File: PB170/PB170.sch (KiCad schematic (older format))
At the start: 30 parts, among them J1 USB_C_Receptacle_USB2.0-Conne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, J2 USB_B_Micro, Q1 P-MOSFET-MLP_HS, Q2 BC817, SW1 SW_MEC_5E, SW2 SW_MEC_5E, U1 74HC00

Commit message: Added PCB.
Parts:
- added H1, H2, H3, H4: MountingHole_Pad, Mounting_Holes:MountingHole_3.2mm_M3_Pad, symbol Mechanical:MountingHole_Pad
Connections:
- wire segments 78 -> 76
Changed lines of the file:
@@
 Wire Wire Line
 	2200 1950 2300 1950
-Wire Wire Line
-	2200 2150 2250 2150
-$Comp
-L power:PWR_FLAG #FLG0101
-U 1 1 5FD0908A
-P 2250 2150
-F 0 "#FLG0101" H 2250 2225 50  0001 C CNN
-F 1 "PWR_FLAG" H 2250 2323 50  0000 C CNN
-F 2 "" H 2250 2150 50  0001 C CNN
-F 3 "~" H 2250 2150 50  0001 C CNN
-	1    2250 2150
-	-1   0    0    1
-$EndComp
-Connection ~ 2250 2150
-Wire Wire Line
-	2250 2150 2300 2150
-$Comp
-L power:PWR_FLAG #FLG0102
-U 1 1 5FD097DA
-P 1300 2100
-F 0 "#FLG0102" H 1300 2175 50  0001 C CNN
-F 1 "PWR_FLAG" H 1300 2273 50  0000 C CNN
-F 2 "" H 1300 2100 50  0001 C CNN
-F 3 "~" H 1300 2100 50  0001 C CNN
-	1    1300 2100
-	-1   0    0    1
-$EndComp
 $Comp
 L power:+5V #PWR0104
@@
 Wire Wire Line
 	1300 2050 1300 2000
-Wire Wire Line
-	1300 2100 1300 2050
-Connection ~ 1300 2050
 Wire Notes Line
 	950  4450 3250 4450
@@
 Wire Wire Line
 	2300 6450 2600 6450
+Wire Wire Line
+	2200 2150 2300 2150
+$Comp
+L Mechanical:MountingHole_Pad H1
+U 1 1 5FD54CAB
+P 4900 7050
+F 0 "H1" H 5000 7099 50  0000 L CNN
+F 1 "MountingHole_Pad" H 5000 7008 50  0000 L CNN
+F 2 "Mounting_Holes:MountingHole_3.2mm_M3_Pad" H 4900 7050 50  0001 C CNN
+F 3 "~" H 4900 7050 50  0001 C CNN
+	1    4900 7050
+	1    0    0    -1
+$EndComp
+$Comp
+L Mechanical:MountingHole_Pad H2
+U 1 1 5FD576B7
+P 5150 7050
+F 0 "H2" H 5250 7099 50  0000 L CNN
+F 1 "MountingHole_Pad" H 5250 7008 50  0000 L CNN
+F 2 "Mounting_Holes:MountingHole_3.2mm_M3_Pad" H 5150 7050 50  0001 C CNN
+F 3 "~" H 5150 7050 50  0001 C CNN
+	1    5150 7050
+	1    0    0    -1
+$EndComp
+$Comp
+L Mechanical:MountingHole_Pad H3
+U 1 1 5FD5794D
+P 5400 7050
+F 0 "H3" H 5500 7099 50  0000 L CNN
+F 1 "MountingHole_Pad" H 5500 7008 50  0000 L CNN
+F 2 "Mounting_Holes:MountingHole_3.2mm_M3_Pad" H 5400 7050 50  0001 C CNN
+F 3 "~" H 5400 7050 50  0001 C CNN
+	1    5400 7050
+	1    0    0    -1
+$EndComp
+$Comp
+L Mechanical:MountingHole_Pad H4
+U 1 1 5FD57BD8
+P 5650 7050
+F 0 "H4" H 5750 7099 50  0000 L CNN
+F 1 "MountingHole_Pad" H 5750 7008 50  0000 L CNN
+F 2 "Mounting_Holes:MountingHole_3.2mm_M3_Pad" H 5650 7050 50  0001 C CNN
+F 3 "~" H 5650 7050 50  0001 C CNN
+	1    5650 7050
+	1    0    0    -1
+$EndComp
 $EndSCHEMATC

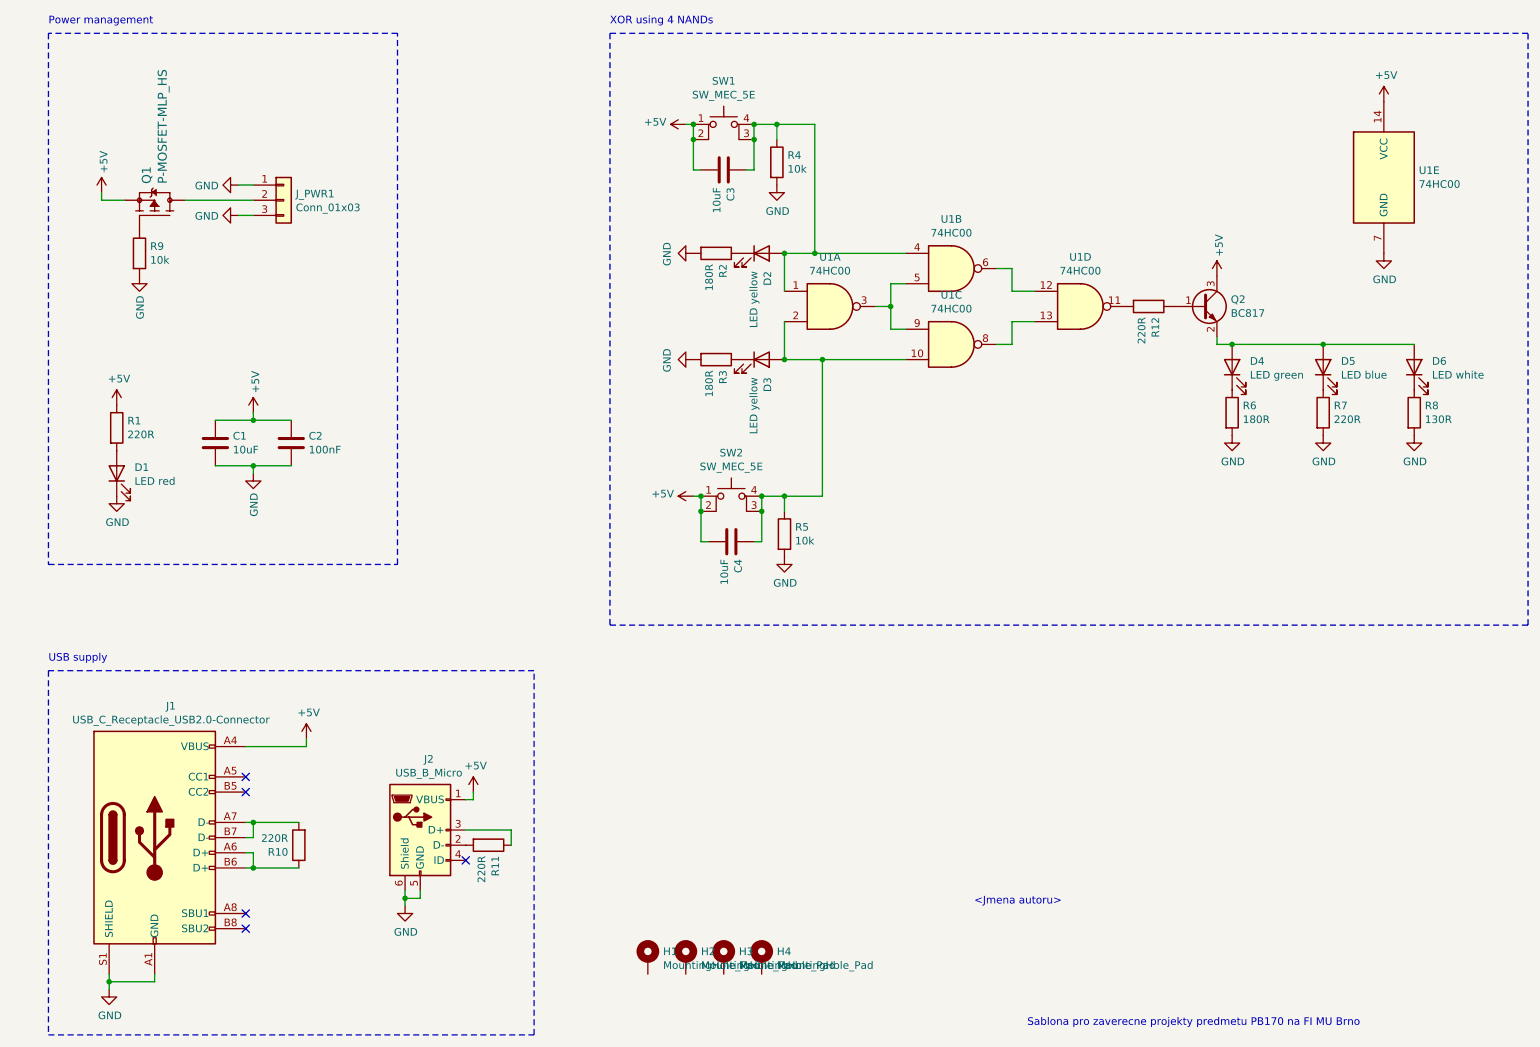
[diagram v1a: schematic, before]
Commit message: Added hierarchical sheet example.
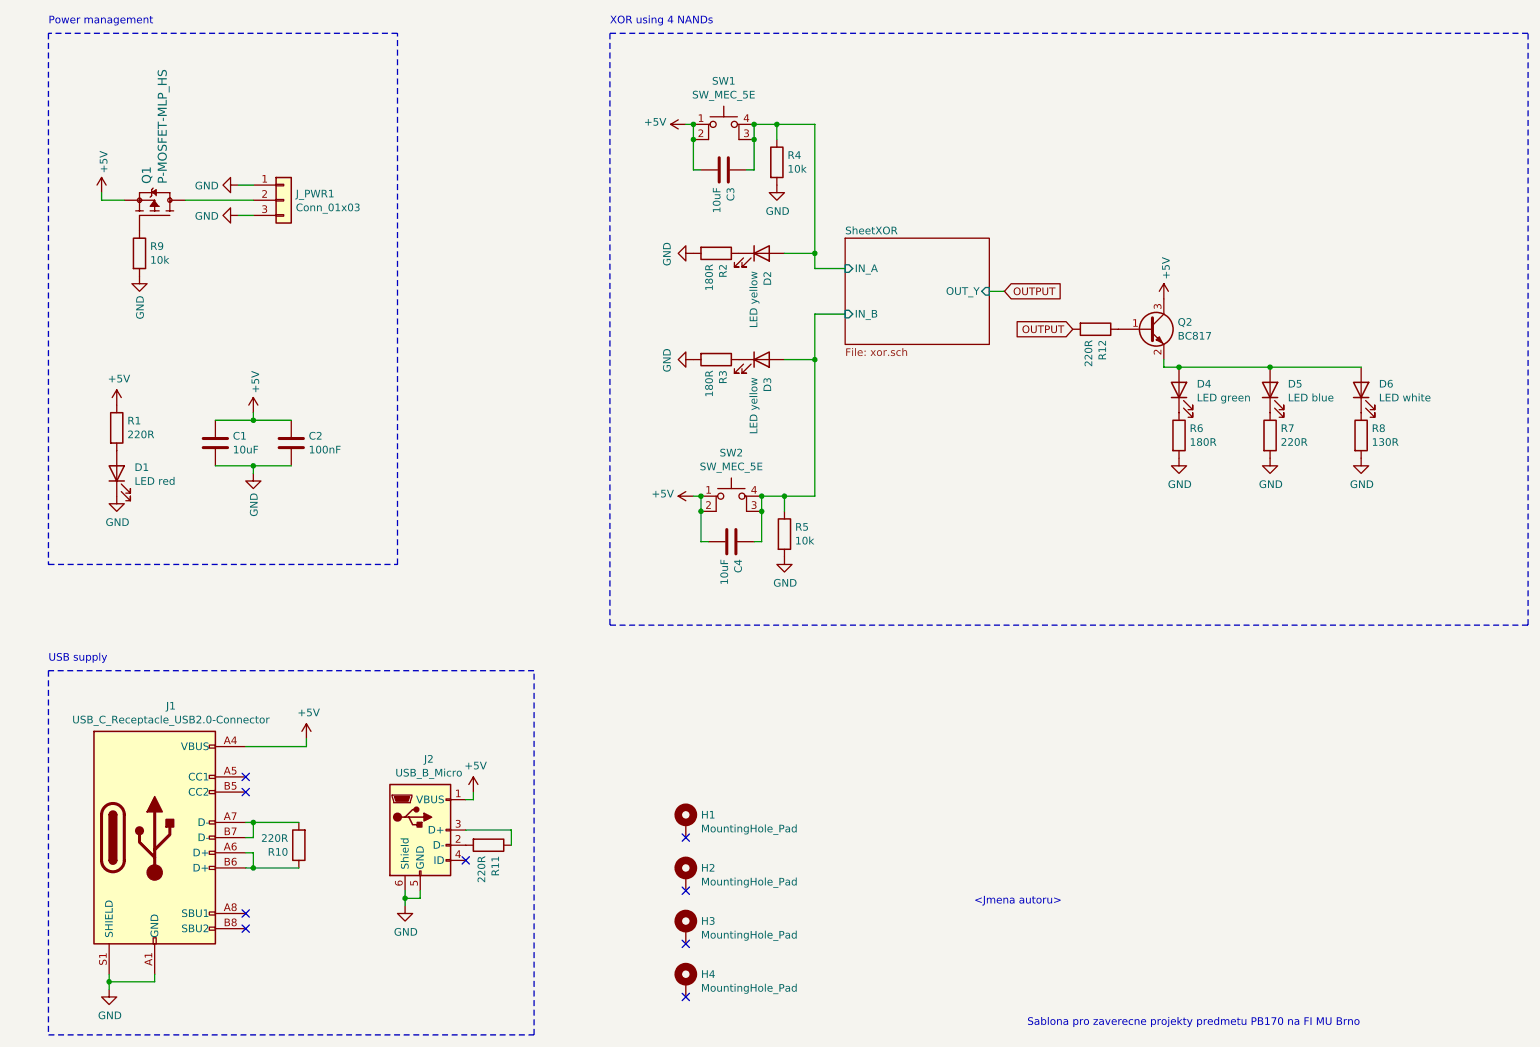
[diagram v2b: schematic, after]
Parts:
- removed U1: 74HC00, Housings_SSOP:TSSOP-14_4.4x5mm_Pitch0.65mm, symbol 74xx:74HC00
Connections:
- net SheetXOR/IN_A: now reaches C3.1, D2.2 (A), R4.1, SW1.3 (K), SW1.4 (A)
- net SheetXOR/IN_B: now reaches C4.1, D3.2 (A), R5.1, SW2.3 (K), SW2.4 (A)
- net OUTPUT: now reaches R12.2
- no-connect marks 5 -> 9
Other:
- moved on the sheet: D4, D5, D6, H1, H2, H3, H4, R12, R6, R7, R8

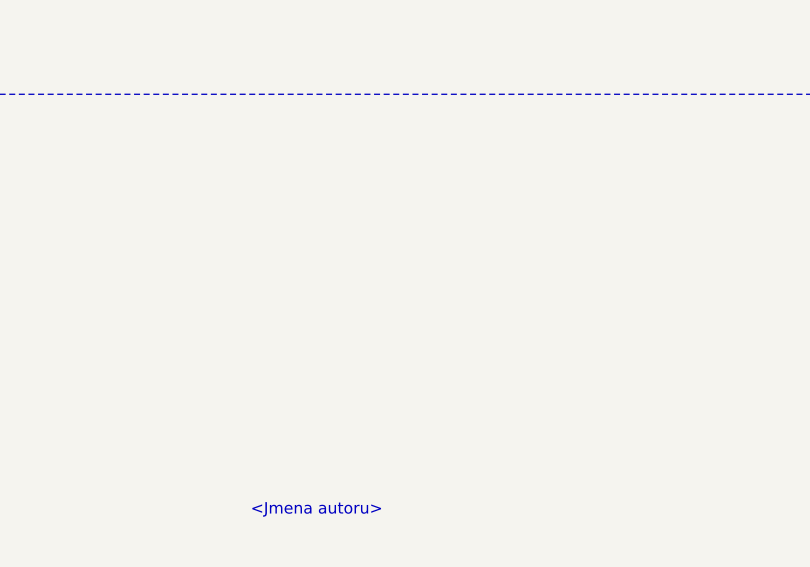
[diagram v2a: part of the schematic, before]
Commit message: Experimentally added 74HC08 symbol.
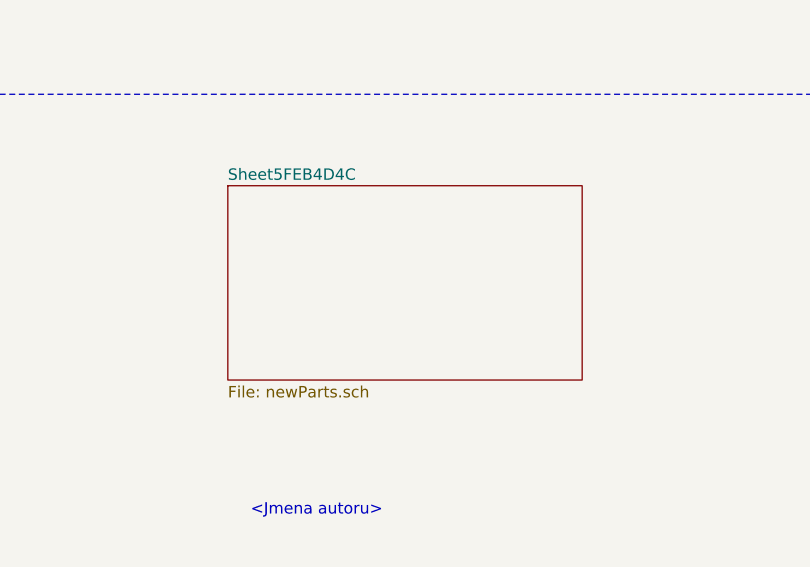
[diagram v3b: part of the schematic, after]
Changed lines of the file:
@@
 $Descr A4 11693 8268
 encoding utf-8
-Sheet 1 2
+Sheet 1 3
 Title ""
 Date ""
@@
 NoConn ~ 5150 6950
 NoConn ~ 5150 7300
+$Sheet
+S 6950 5250 1550 850
+U 5FEB4D4D
+F0 "Sheet5FEB4D4C" 50
+F1 "newParts.sch" 50
+$EndSheet
 $EndSCHEMATC

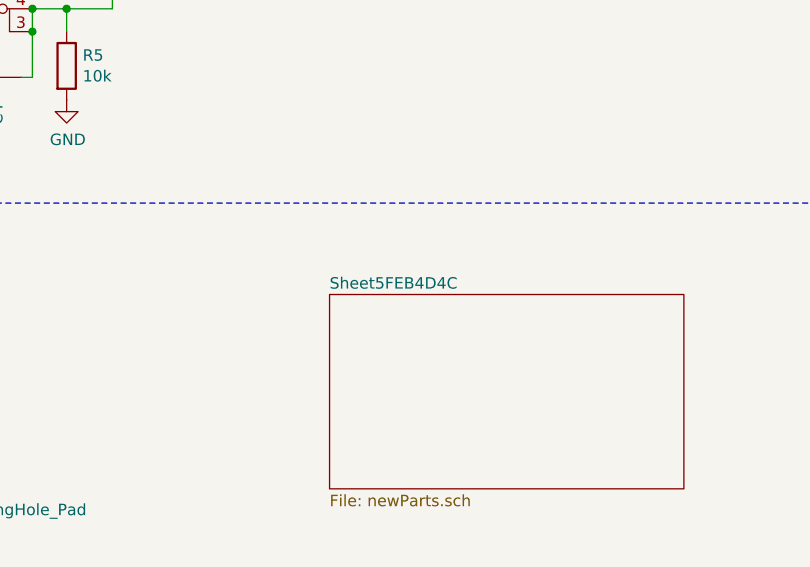
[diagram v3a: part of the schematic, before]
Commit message: Added sample OR gate 74HC32.
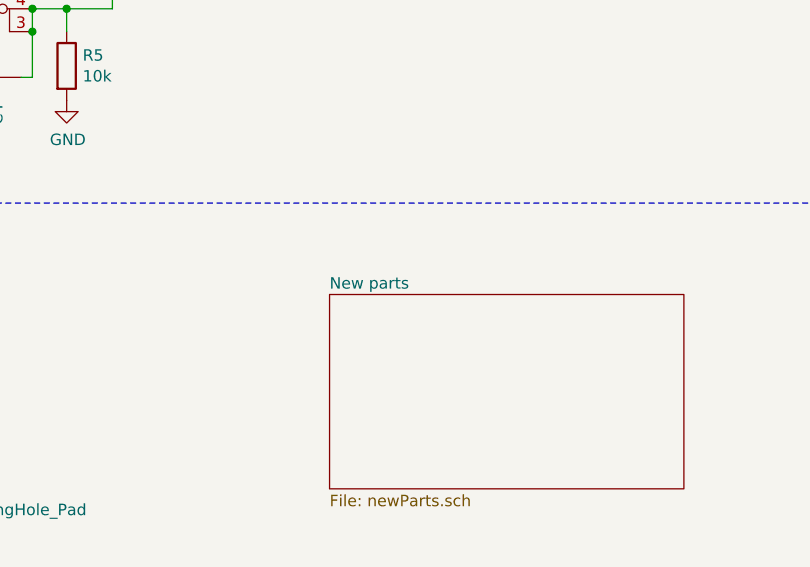
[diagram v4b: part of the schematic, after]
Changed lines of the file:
@@
 S 6950 5250 1550 850
 U 5FEB4D4D
-F0 "Sheet5FEB4D4C" 50
+F0 "New parts" 50
 F1 "newParts.sch" 50
 $EndSheet

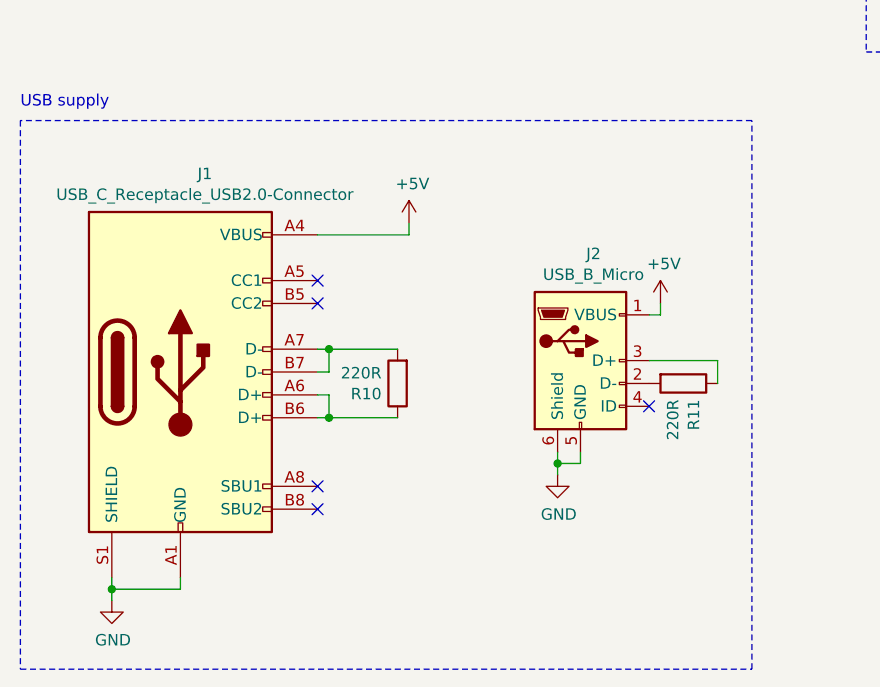
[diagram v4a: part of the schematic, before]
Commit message: Created examples with new THT parts.
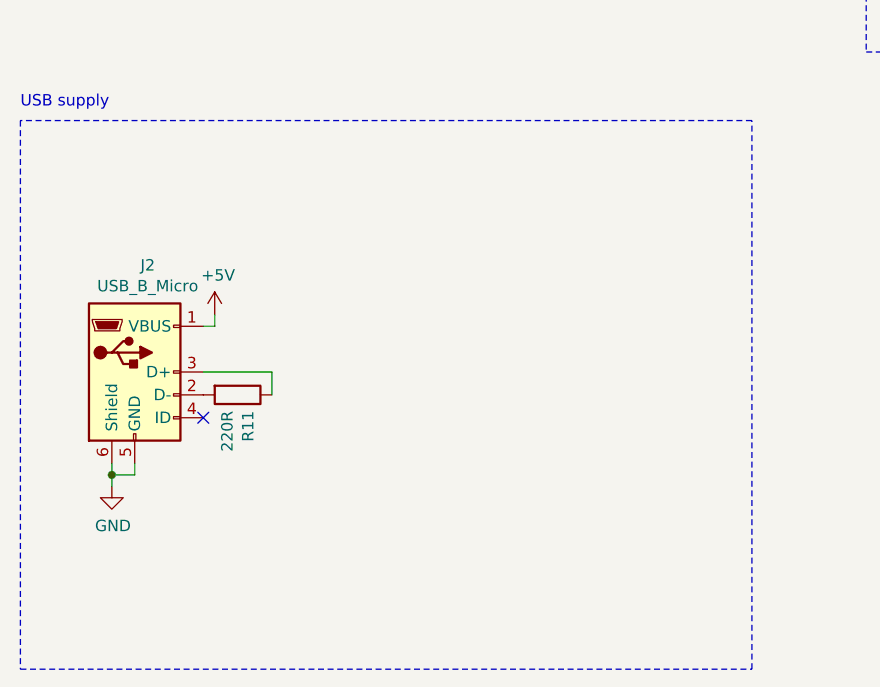
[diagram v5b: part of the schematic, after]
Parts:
- removed J1: USB_C_Receptacle_USB2.0-Connector, PB170:USB_C_Female-16Pin-HPJF, symbol PB170:USB_C_Receptacle_USB2.0-Connector
- removed R10: 220R, Resistors_SMD:R_0603, symbol Device:R
- J2: footprint PB170:USB_Micro-B_Wuerth_629105150521_CircularHoles -> PB170:MICRO-USB-SMD_MICROXNJ; LCSC (none) -> C404969
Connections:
- no-connect marks 9 -> 5
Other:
- moved on the sheet: J2, R11
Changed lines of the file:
@@
 L Connector:USB_B_Micro J2
 U 1 1 5FD07183
-P 3400 6200
-F 0 "J2" H 3457 6667 50  0000 C CNN
-F 1 "USB_B_Micro" H 3457 6576 50  0000 C CNN
-F 2 "PB170:USB_Micro-B_Wuerth_629105150521_CircularHoles" H 3550 6150 50  0001 C CNN
-F 3 "~" H 3550 6150 50  0001 C CNN
-	1    3400 6200
+P 1450 6250
+F 0 "J2" H 1507 6717 50  0000 C CNN
+F 1 "USB_B_Micro" H 1507 6626 50  0000 C CNN
+F 2 "PB170:MICRO-USB-SMD_MICROXNJ" H 1600 6200 50  0001 C CNN
+F 3 "https://datasheet.lcsc.com/szlcsc/1912111437_SHOU-HAN-MicroXNJ_C404969.pdf" H 1600 6200 50  0001 C CNN
+F 4 "C404969" H 1450 6250 50  0001 C CNN "LCSC"
+	1    1450 6250
 	1    0    0    -1
 $EndComp
@@
 L Device:R R11
 U 1 1 5FD41C51
-P 3850 6300
-F 0 "R11" H 3920 6346 50  0000 L CNN
-F 1 "220R" H 3920 6255 50  0000 L CNN
-F 2 "Resistors_SMD:R_0603" V 3780 6300 50  0001 C CNN
-F 3 "https://datasheet.lcsc.com/szlcsc/Uniroyal-Elec-0603WAF2200T5E_C22962.pdf" H 3850 6300 50  0001 C CNN
-F 4 "C22962" H 3850 6300 50  0001 C CNN "LCSC"
-	1    3850 6300
+P 1900 6350
+F 0 "R11" H 1970 6396 50  0000 L CNN
+F 1 "220R" H 1970 6305 50  0000 L CNN
+F 2 "Resistors_SMD:R_0603" V 1830 6350 50  0001 C CNN
+F 3 "https://datasheet.lcsc.com/szlcsc/Uniroyal-Elec-0603WAF2200T5E_C22962.pdf" H 1900 6350 50  0001 C CNN
+F 4 "C22962" H 1900 6350 50  0001 C CNN "LCSC"
+	1    1900 6350
 	0    1    1    0
 $EndComp
 Wire Wire Line
-	3700 6200 4000 6200
+	1750 6250 2050 6250
 Wire Wire Line
-	4000 6200 4000 6300
+	2050 6250 2050 6350
 $Comp
 L power:GND #PWR0121
 U 1 1 5FD447F1
-P 3300 6700
-F 0 "#PWR0121" H 3300 6450 50  0001 C CNN
-F 1 "GND" H 3305 6527 50  0000 C CNN
-F 2 "" H 3300 6700 50  0001 C CNN
-F 3 "" H 3300 6700 50  0001 C CNN
-	1    3300 6700
+P 1350 6750
+F 0 "#PWR0121" H 1350 6500 50  0001 C CNN
+F 1 "GND" H 1355 6577 50  0000 C CNN
+F 2 "" H 1350 6750 50  0001 C CNN
+F 3 "" H 1350 6750 50  0001 C CNN
+	1    1350 6750
 	1    0    0    -1
 $EndComp
 Wire Wire Line
-	3300 6700 3300 6650
+	1350 6750 1350 6700
 Wire Wire Line
-	3400 6600 3400 6650
+	1450 6650 1450 6700
 Wire Wire Line
-	3400 6650 3300 6650
-Connection ~ 3300 6650
+	1450 6700 1350 6700
+Connection ~ 1350 6700
 Wire Wire Line
-	3300 6650 3300 6600
+	1350 6700 1350 6650
 $Comp
 L power:+5V #PWR0122
 U 1 1 5FD489FB
-P 3750 5950
-F 0 "#PWR0122" H 3750 5800 50  0001 C CNN
-F 1 "+5V" H 3765 6123 50  0000 C CNN
-F 2 "" H 3750 5950 50  0001 C CNN
-F 3 "" H 3750 5950 50  0001 C CNN
-	1    3750 5950
+P 1800 6000
+F 0 "#PWR0122" H 1800 5850 50  0001 C CNN
+F 1 "+5V" H 1815 6173 50  0000 C CNN
+F 2 "" H 1800 6000 50  0001 C CNN
+F 3 "" H 1800 6000 50  0001 C CNN
+	1    1800 6000
 	1    0    0    -1
 $EndComp
 Wire Wire Line
-	3700 6000 3750 6000
+	1750 6050 1800 6050
 Wire Wire Line
-	3750 6000 3750 5950
-$Comp
-L power:GND #PWR0123
-U 1 1 5FD4C7CC
-P 1350 7250
-F 0 "#PWR0123" H 1350 7000 50  0001 C CNN
-F 1 "GND" H 1355 7077 50  0000 C CNN
-F 2 "" H 1350 7250 50  0001 C CNN
-F 3 "" H 1350 7250 50  0001 C CNN
-	1    1350 7250
-	1    0    0    -1
-$EndComp
-$Comp
-L Device:R R10
-U 1 1 5FD50BFB
-P 2600 6300
-F 0 "R10" H 2670 6346 50  0000 L CNN
-F 1 "220R" H 2670 6255 50  0000 L CNN
-F 2 "Resistors_SMD:R_0603" V 2530 6300 50  0001 C CNN
-F 3 "https://datasheet.lcsc.com/szlcsc/Uniroyal-Elec-0603WAF2200T5E_C22962.pdf" H 2600 6300 50  0001 C CNN
-F 4 "C22962" H 2600 6300 50  0001 C CNN "LCSC"
-	1    2600 6300
-	-1   0    0    1
-$EndComp
-Wire Wire Line
-	2250 6150 2300 6150
-Wire Wire Line
-	2250 6450 2300 6450
-$Comp
-L power:+5V #PWR0124
-U 1 1 5FD594C3
-P 2650 5600
-F 0 "#PWR0124" H 2650 5450 50  0001 C CNN
-F 1 "+5V" H 2665 5773 50  0000 C CNN
-F 2 "" H 2650 5600 50  0001 C CNN
-F 3 "" H 2650 5600 50  0001 C CNN
-	1    2650 5600
-	1    0    0    -1
-$EndComp
+	1800 6050 1800 6000
 Wire Notes Line
 	4650 950  4650 4850
@@
 Wire Notes Line
 	4150 5150 950  5150
-NoConn ~ 3700 6400
+NoConn ~ 1750 6450
 Text Notes 7400 7500 0    50   ~ 0
 Sablona pro zaverecne projekty predmetu PB170 na FI MU Brno
@@
 Text Notes 4650 900  0    50   ~ 0
 XOR using 4 NANDs
-$Comp
-L PB170:USB_C_Receptacle_USB2.0-Connector J1
-U 1 1 5FD02084
-P 1650 6250
-F 0 "J1" H 1757 7117 50  0000 C CNN
-F 1 "USB_C_Receptacle_USB2.0-Connector" H 1757 7026 50  0000 C CNN
-F 2 "PB170:USB_C_Female-16Pin-HPJF" H 1800 6250 50  0001 C CNN
-F 3 "" H 1800 6250 50  0001 C CNN
-	1    1650 6250
-	1    0    0    -1
-$EndComp
-Wire Wire Line
-	1350 7250 1350 7200
-Wire Wire Line
-	1650 7150 1650 7200
-Wire Wire Line
-	1650 7200 1350 7200
-Connection ~ 1350 7200
-Wire Wire Line
-	1350 7200 1350 7150
-Wire Wire Line
-	2250 5650 2650 5650
-Wire Wire Line
-	2650 5650 2650 5600
-NoConn ~ 2250 5850
-NoConn ~ 2250 5950
-NoConn ~ 2250 6750
-NoConn ~ 2250 6850
-Wire Wire Line
-	2250 6250 2300 6250
-Wire Wire Line
-	2300 6250 2300 6150
-Connection ~ 2300 6150
-Wire Wire Line
-	2300 6150 2600 6150
-Wire Wire Line
-	2250 6350 2300 6350
-Wire Wire Line
-	2300 6350 2300 6450
-Connection ~ 2300 6450
-Wire Wire Line
-	2300 6450 2600 6450
 Wire Wire Line
 	2200 2150 2300 2150
